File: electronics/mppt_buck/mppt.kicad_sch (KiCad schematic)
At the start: 49 parts, among them J1 I2C, J2 UART, J3 In, J4 In, J5 Out, J6 Out, Q1 IRLR2705TRPBF, Q2 IRLR2705TRPBF, SW1 SW_DIP_x01, U1 AD8211, U2 AD8211, U3 ATmega328P-A, U4 2EDN852x, U5 L78L15_SO8, Y1 16.00M-SMDHC49S

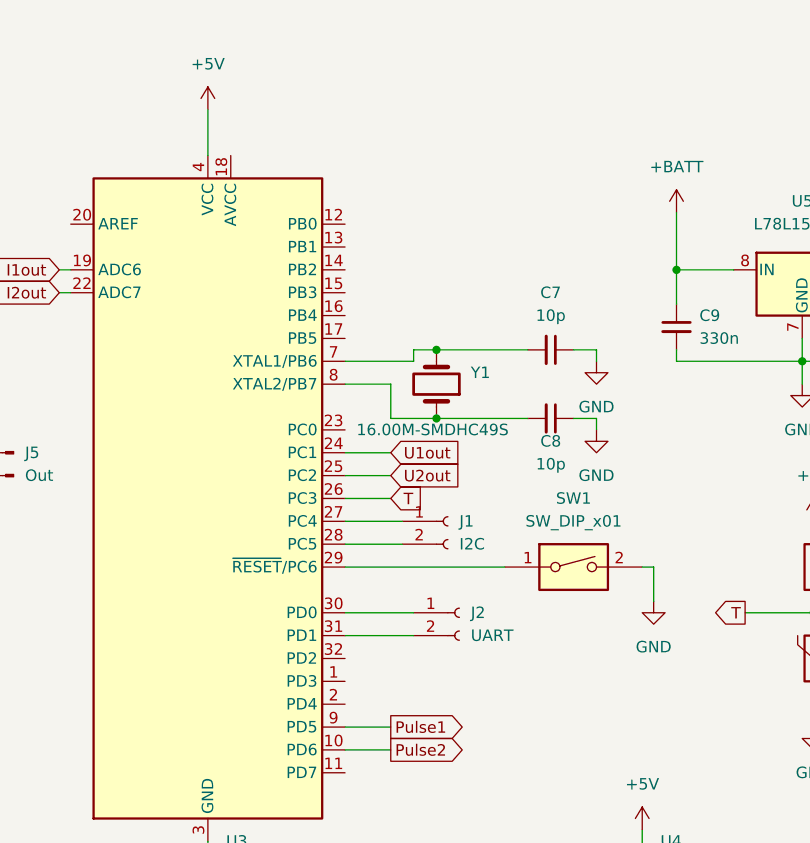
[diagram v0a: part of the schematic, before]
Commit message: mppt cpu reset fix
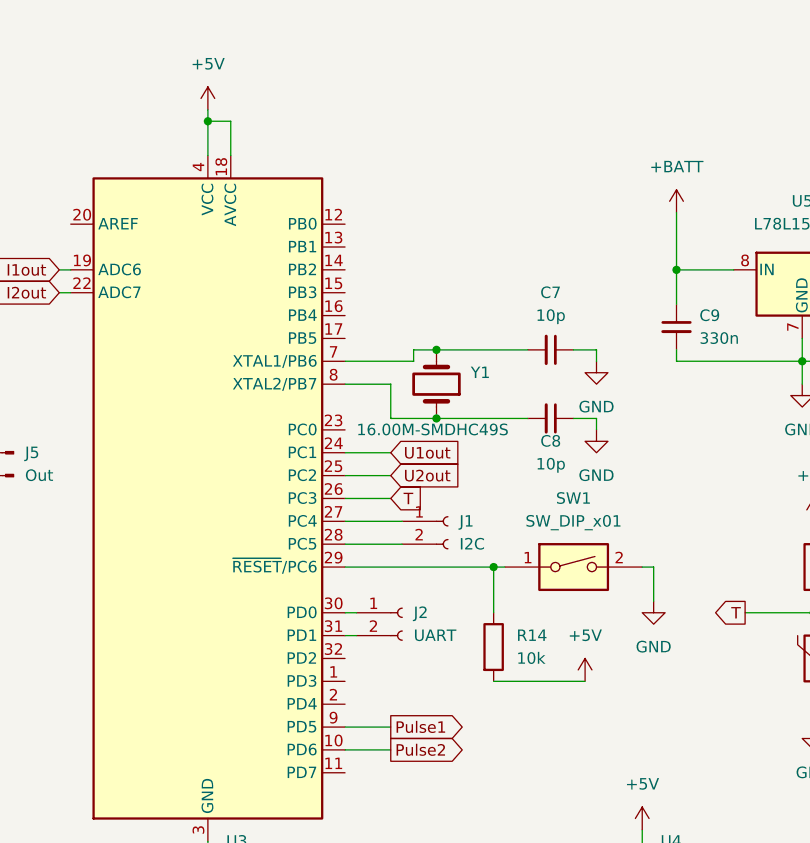
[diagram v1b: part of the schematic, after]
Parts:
- added R14: 10k, Resistor_SMD:R_1206_3216Metric_Pad1.30x1.75mm_HandSolder, symbol Device:R
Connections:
- net +5V: now also U3.18 (AVCC), R14.2
- net at SW1.1, U3.29 (~{RESET}/PC6): now also R14.1
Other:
- moved on the sheet: J2
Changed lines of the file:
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@@
   (junction (at 153.67 152.4) (diameter 0) (color 0 0 0 0)
   )
+  (junction (at 228.6 80.01) (diameter 0) (color 0 0 0 0)
+  )
   (junction (at 222.25 55.88) (diameter 0) (color 0 0 0 0)
   )
@@
   (junction (at 24.13 58.42) (diameter 0) (color 0 0 0 0)
   )
+  (junction (at 196.85 30.48) (diameter 0) (color 0 0 0 0)
+  )
   (junction (at 72.39 58.42) (diameter 0) (color 0 0 0 0)
   )
@@
     (stroke (width 0) (type default) (color 0 0 0 0))
   )
+  (wire (pts (xy 228.6 92.71) (xy 238.76 92.71))
+    (stroke (width 0) (type default) (color 0 0 0 0))
+  )
+  (wire (pts (xy 228.6 80.01) (xy 229.87 80.01))
+    (stroke (width 0) (type default) (color 0 0 0 0))
+  )
   (wire (pts (xy 152.4 58.42) (xy 170.18 58.42))
     (stroke (width 0) (type default) (color 0 0 0 0))
@@
     (stroke (width 0) (type default) (color 0 0 0 0))
   )
-  (wire (pts (xy 212.09 80.01) (xy 229.87 80.01))
+  (wire (pts (xy 212.09 80.01) (xy 228.6 80.01))
     (stroke (width 0) (type default) (color 0 0 0 0))
   )
@@
     (stroke (width 0) (type default) (color 0 0 0 0))
   )
-  (wire (pts (xy 212.09 87.63) (xy 219.71 87.63))
+  (wire (pts (xy 212.09 87.63) (xy 213.36 87.63))
     (stroke (width 0) (type default) (color 0 0 0 0))
   )
@@
     (stroke (width 0) (type default) (color 0 0 0 0))
   )
-  (wire (pts (xy 212.09 85.09) (xy 219.71 85.09))
+  (wire (pts (xy 212.09 85.09) (xy 213.36 85.09))
     (stroke (width 0) (type default) (color 0 0 0 0))
   )
@@
     (stroke (width 0) (type default) (color 0 0 0 0))
   )
+  (wire (pts (xy 199.39 30.48) (xy 196.85 30.48))
+    (stroke (width 0) (type default) (color 0 0 0 0))
+  )
   (wire (pts (xy 153.67 129.54) (xy 172.72 129.54))
     (stroke (width 0) (type default) (color 0 0 0 0))
@@
     (stroke (width 0) (type default) (color 0 0 0 0))
   )
+  (wire (pts (xy 228.6 80.01) (xy 228.6 85.09))
+    (stroke (width 0) (type default) (color 0 0 0 0))
+  )
   (wire (pts (xy 170.18 69.85) (xy 170.18 81.28))
     (stroke (width 0) (type default) (color 0 0 0 0))
@@
     (stroke (width 0) (type default) (color 0 0 0 0))
   )
-  (wire (pts (xy 196.85 29.21) (xy 196.85 34.29))
+  (wire (pts (xy 196.85 29.21) (xy 196.85 30.48))
     (stroke (width 0) (type default) (color 0 0 0 0))
   )
@@
     (stroke (width 0) (type default) (color 0 0 0 0))
   )
+  (wire (pts (xy 199.39 34.29) (xy 199.39 30.48))
+    (stroke (width 0) (type default) (color 0 0 0 0))
+  )
   (wire (pts (xy 219.71 55.88) (xy 219.71 57.15))
     (stroke (width 0) (type default) (color 0 0 0 0))
@@
   )
   (wire (pts (xy 180.34 46.99) (xy 181.61 46.99))
+    (stroke (width 0) (type default) (color 0 0 0 0))
+  )
+  (wire (pts (xy 196.85 30.48) (xy 196.85 34.29))
     (stroke (width 0) (type default) (color 0 0 0 0))
   )
@@
     (pin "2")
   )
-  (symbol (lib_id "Connector:Conn_01x02_Female") (at 224.79 85.09 0) (unit 1)
-    (in_bom yes) (on_board yes) (fields_autoplaced)
-    (property "Reference" "J2" (id 0) (at 226.06 85.0899 0)
-      (effects (font (size 1.27 1.27)) (justify left))
-    )
-    (property "Value" "UART" (id 1) (at 226.06 87.6299 0)
-      (effects (font (size 1.27 1.27)) (justify left))
-    )
-    (property "Footprint" "Connector_Wire:SolderWire-1.5sqmm_1x02_P7.8mm_D1.7mm_OD3.9mm" (id 2) (at 224.79 85.09 0)
-      (effects (font (size 1.27 1.27)) hide)
-    )
-    (property "Datasheet" "~" (id 3) (at 224.79 85.09 0)
+  (symbol (lib_id "Connector:Conn_01x02_Female") (at 218.44 85.09 0) (unit 1)
+    (in_bom yes) (on_board yes) (fields_autoplaced)
+    (property "Reference" "J2" (id 0) (at 219.71 85.0899 0)
+      (effects (font (size 1.27 1.27)) (justify left))
+    )
+    (property "Value" "UART" (id 1) (at 219.71 87.6299 0)
+      (effects (font (size 1.27 1.27)) (justify left))
+    )
+    (property "Footprint" "Connector_Wire:SolderWire-1.5sqmm_1x02_P7.8mm_D1.7mm_OD3.9mm" (id 2) (at 218.44 85.09 0)
+      (effects (font (size 1.27 1.27)) hide)
+    )
+    (property "Datasheet" "~" (id 3) (at 218.44 85.09 0)
       (effects (font (size 1.27 1.27)) hide)
     )
@@
     (pin "2")
   )
+  (symbol (lib_id "power:+5V") (at 238.76 92.71 0) (unit 1)
+    (in_bom yes) (on_board yes) (fields_autoplaced)
+    (property "Reference" "#PWR01" (id 0) (at 238.76 96.52 0)
+      (effects (font (size 1.27 1.27)) hide)
+    )
+    (property "Value" "+5V" (id 1) (at 238.76 87.63 0))
+    (property "Footprint" "" (id 2) (at 238.76 92.71 0)
+      (effects (font (size 1.27 1.27)) hide)
+    )
+    (property "Datasheet" "" (id 3) (at 238.76 92.71 0)
+      (effects (font (size 1.27 1.27)) hide)
+    )
+    (pin "1")
+  )
   (symbol (lib_id "power:GND") (at 196.85 114.3 0) (unit 1)
     (in_bom yes) (on_board yes) (fields_autoplaced)
@@
     )
     (pin "1")
+  )
+  (symbol (lib_id "Device:R") (at 228.6 88.9 0) (unit 1)
+    (in_bom yes) (on_board yes) (fields_autoplaced)
+    (property "Reference" "R14" (id 0) (at 231.14 87.6299 0)
+      (effects (font (size 1.27 1.27)) (justify left))
+    )
+    (property "Value" "10k" (id 1) (at 231.14 90.1699 0)
+      (effects (font (size 1.27 1.27)) (justify left))
+    )
+    (property "Footprint" "Resistor_SMD:R_1206_3216Metric_Pad1.30x1.75mm_HandSolder" (id 2) (at 226.822 88.9 90)
+      (effects (font (size 1.27 1.27)) hide)
+    )
+    (property "Datasheet" "https://www.tme.eu/pl/details/wr12x1002ftl/rezystory-smd-1206/walsin/" (id 3) (at 228.6 88.9 0)
+      (effects (font (size 1.27 1.27)) hide)
+    )
+    (pin "1")
+    (pin "2")
   )
   (symbol (lib_id "Switch:SW_DIP_x01") (at 237.49 80.01 0) (unit 1)
@@
   )
   (symbol_instances
+    (path "/c6a816bb-f5db-43ba-b9aa-d906c309208d"
+      (reference "#PWR01") (unit 1) (value "+5V") (footprint "")
+    )
     (path "/4e01f4b2-cdfb-4e3f-ab27-647ac2d75ef1"
       (reference "#PWR03") (unit 1) (value "VCC") (footprint "")
@@
       (reference "R13") (unit 1) (value "100k") (footprint "Resistor_SMD:R_1206_3216Metric_Pad1.30x1.75mm_HandSolder")
     )
+    (path "/cf9aa3b6-c2bb-4046-afae-9eb65d930a97"
+      (reference "R14") (unit 1) (value "10k") (footprint "Resistor_SMD:R_1206_3216Metric_Pad1.30x1.75mm_HandSolder")
+    )
     (path "/d39a6313-1ab9-4ec3-80c7-c6ab9bb1690b"
